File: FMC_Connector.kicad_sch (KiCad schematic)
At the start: 2 parts, among them J1 ASP-134488-01

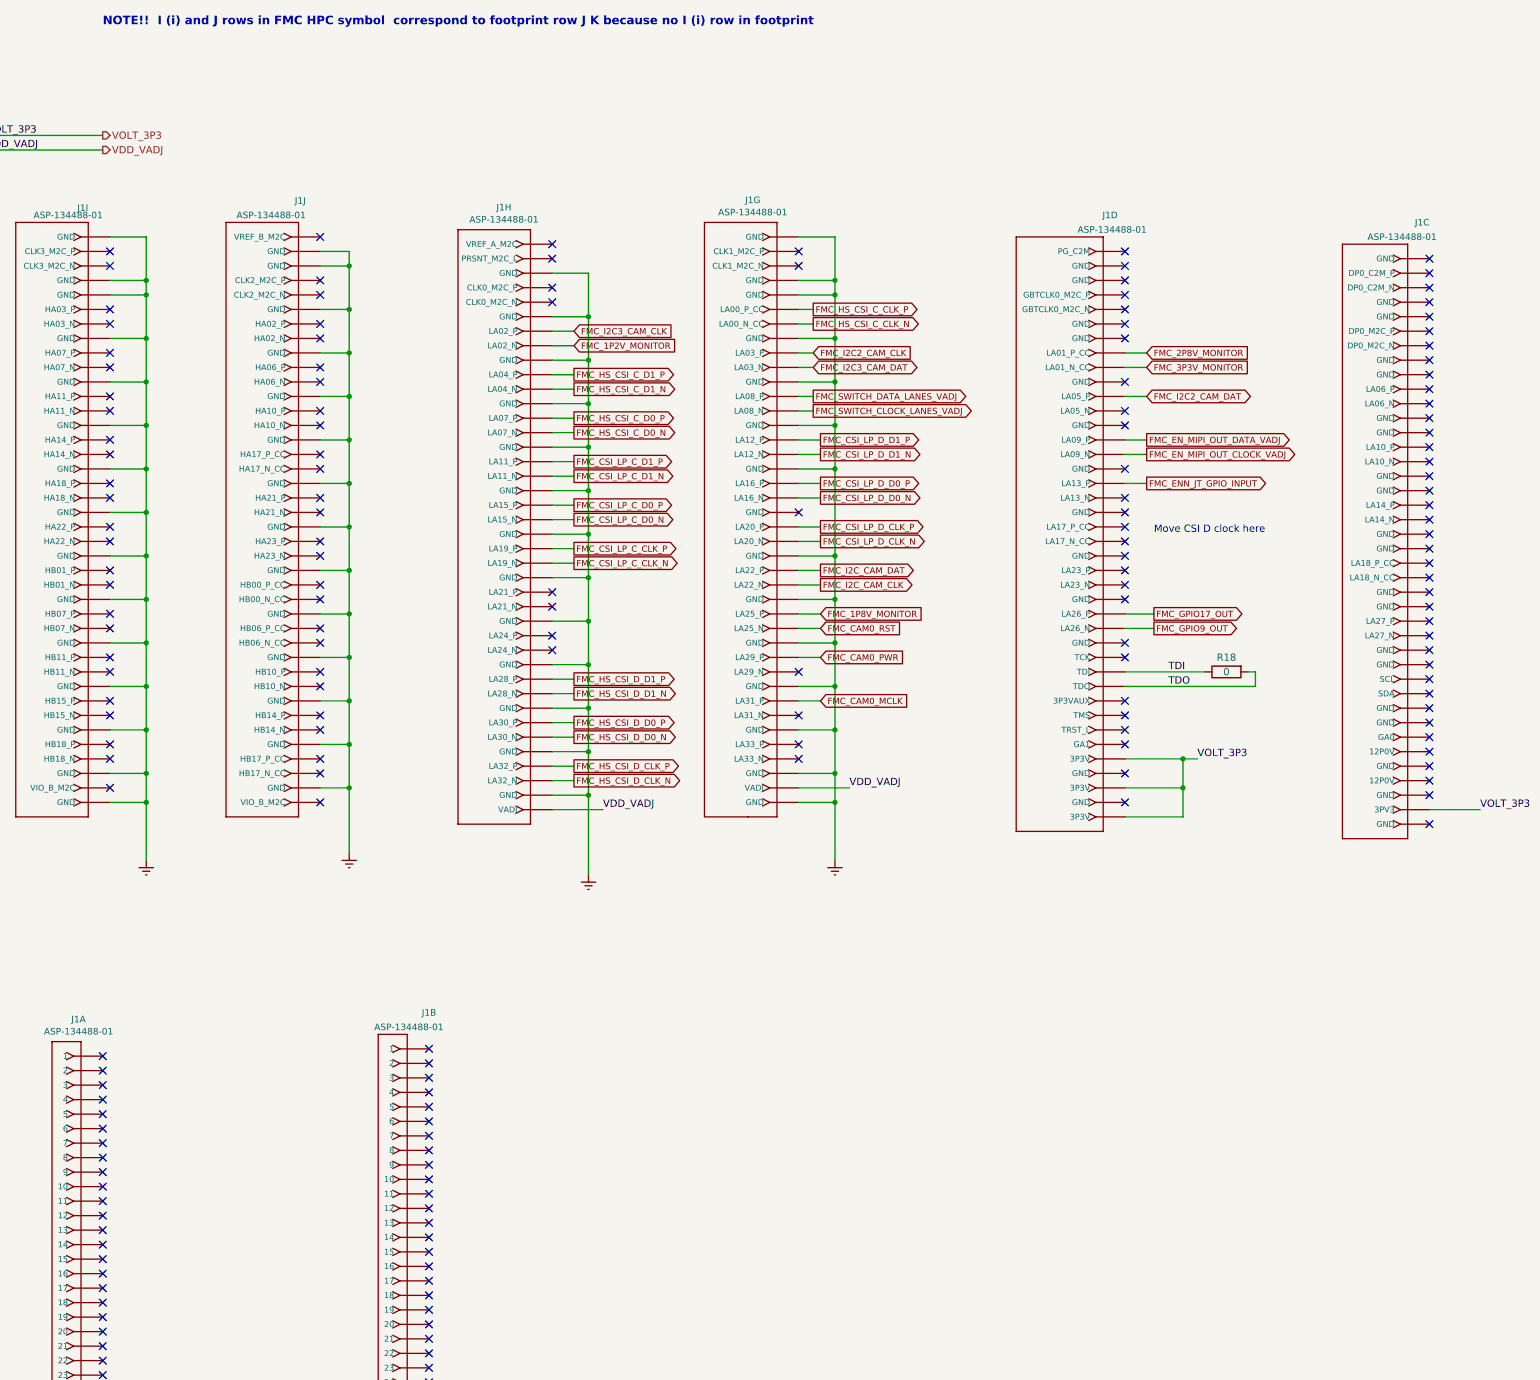
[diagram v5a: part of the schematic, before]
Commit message: Added debug points
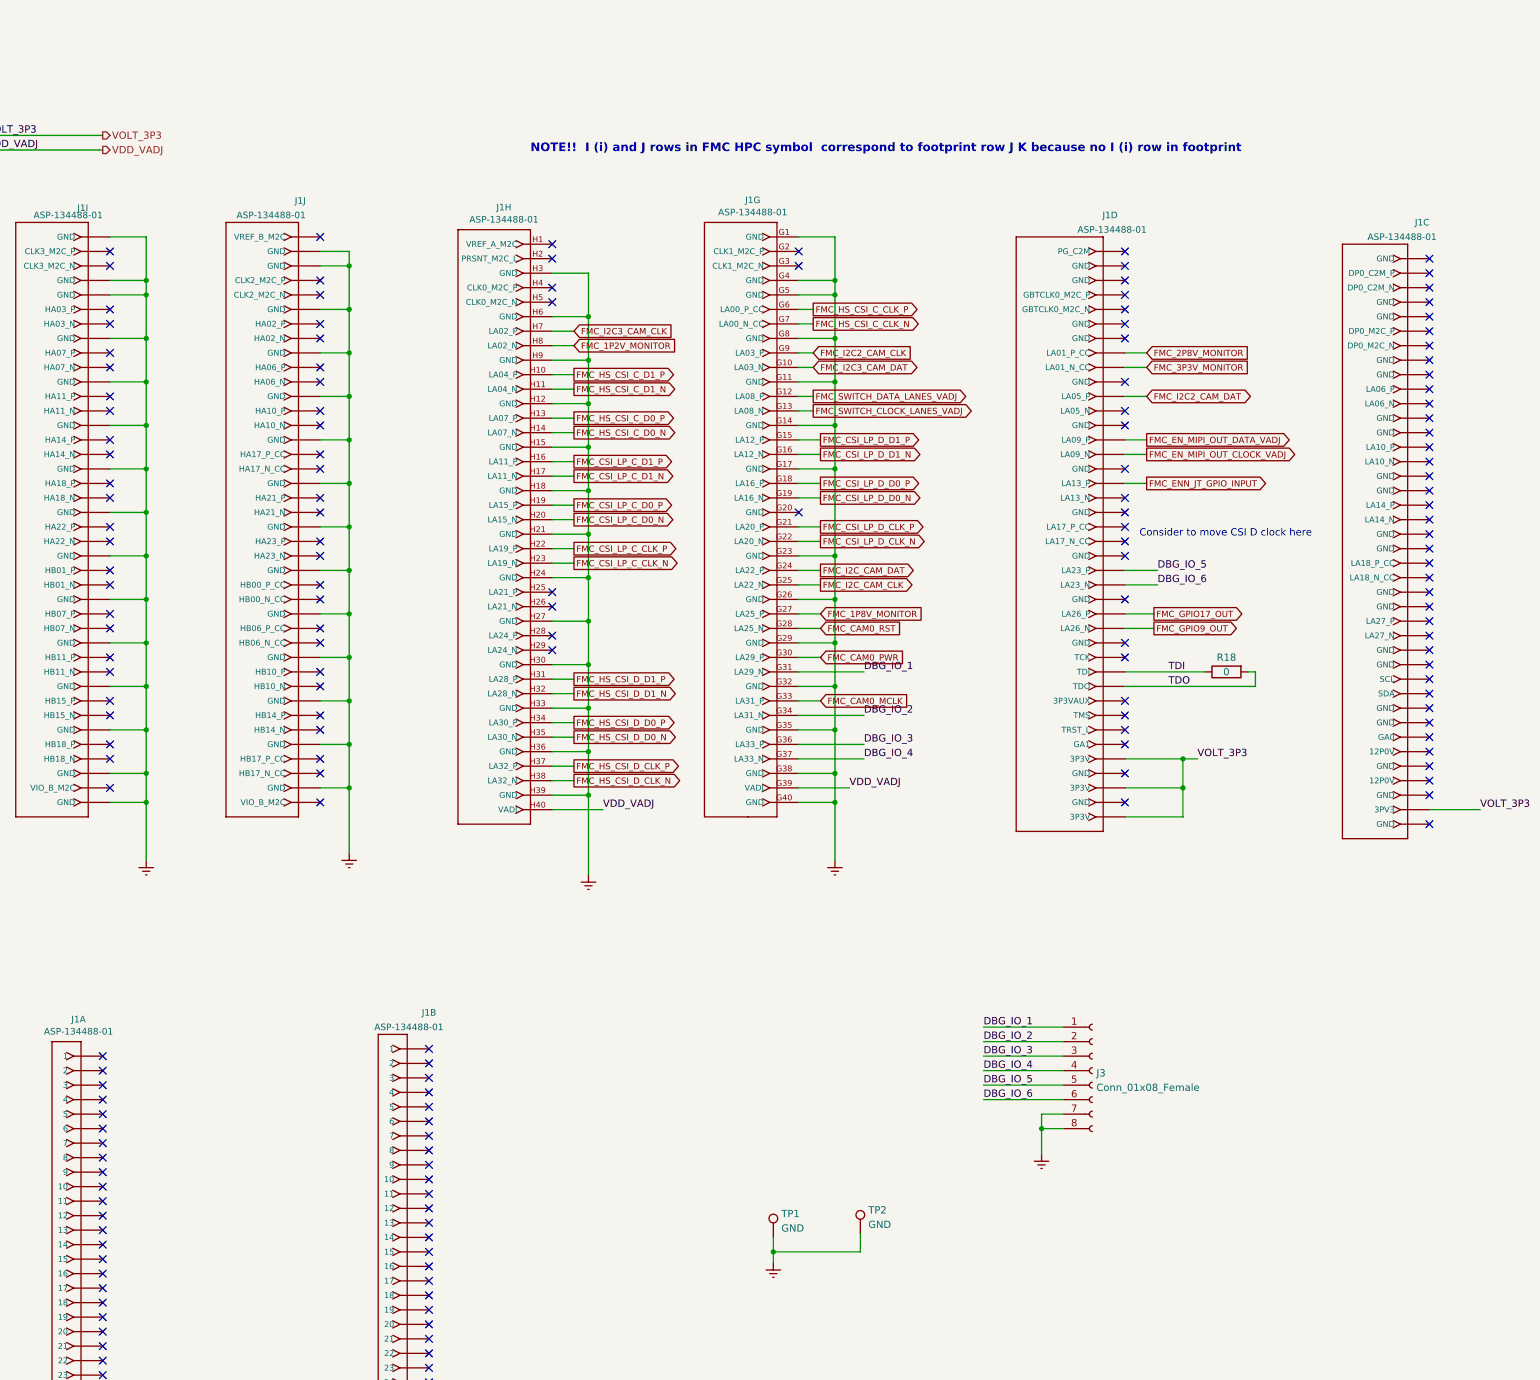
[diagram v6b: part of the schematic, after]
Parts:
- added J3: Conn_01x08_Female, Connector_PinHeader_2.54mm:PinHeader_2x04_P2.54mm_Vertical, symbol Connector:Conn_01x08_Female
- added TP1, TP2: GND, TestPoint:TestPoint_Keystone_5010-5014_Multipurpose, symbol Connector:TestPoint
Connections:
- net Earth: now also J3.7 (Pin_7), J3.8 (Pin_8), TP1.1, TP2.1
- net DBG_IO_5: now reaches J1.D23 (LA23_P)
- net DBG_IO_5: now also J3.5 (Pin_5)
- net DBG_IO_6: now reaches J1.D24 (LA23_N)
- net DBG_IO_6: now also J3.6 (Pin_6)
- net DBG_IO_1: now reaches J1.G31 (LA29_N)
- net DBG_IO_1: now also J3.1 (Pin_1)
- net DBG_IO_2: now reaches J1.G34 (LA31_N)
- net DBG_IO_2: now also J3.2 (Pin_2)
- net DBG_IO_3: now reaches J1.G36 (LA33_P)
- net DBG_IO_3: now also J3.3 (Pin_3)
- net DBG_IO_4: now reaches J1.G37 (LA33_N)
- net DBG_IO_4: now also J3.4 (Pin_4)
- no-connect marks 261 -> 255
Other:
- note added: "Consider to move CSI D clock here"
- note removed: "Move CSI D clock here"

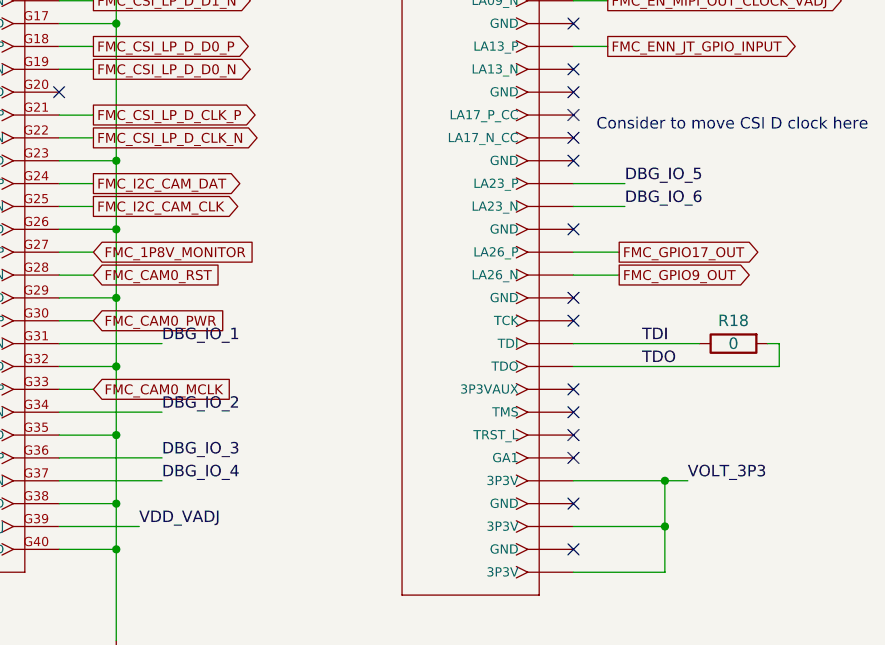
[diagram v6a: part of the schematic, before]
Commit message: Added debug connector
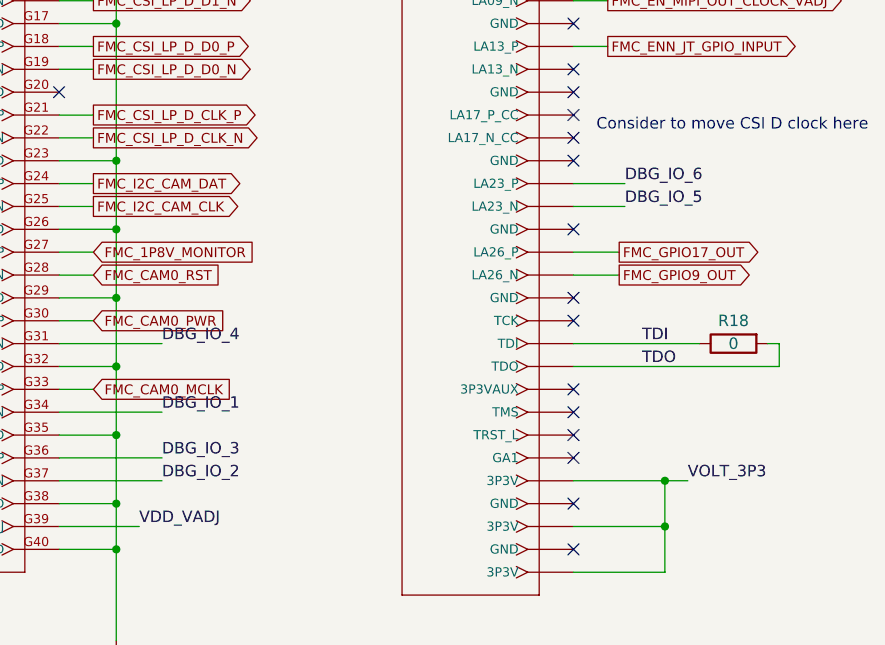
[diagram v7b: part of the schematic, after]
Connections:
- net DBG_IO_1: now also J1.G34 (LA31_N); no longer J1.G31 (LA29_N)
- net DBG_IO_2: now also J1.G37 (LA33_N); no longer J1.G34 (LA31_N)
- net DBG_IO_4: now also J1.G31 (LA29_N); no longer J1.G37 (LA33_N)
- net DBG_IO_5: now also J1.D24 (LA23_N); no longer J1.D23 (LA23_P)
- net DBG_IO_6: now also J1.D23 (LA23_P); no longer J1.D24 (LA23_N)
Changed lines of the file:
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@@
+    (effects (font (size 1.27 1.27)) (justify left bottom))
+  )
+  (label "DBG_IO_1" (at 168.91 118.11 0)
+    (effects (font (size 1.27 1.27)) (justify left bottom))
+  )
+  (label "DBG_IO_5" (at 220.345 95.25 0)
     (effects (font (size 1.27 1.27)) (justify left bottom))
   )
@@
     (effects (font (size 1.27 1.27)) (justify left bottom))
   )
-  (label "DBG_IO_5" (at 220.345 92.71 0)
+  (label "DBG_IO_3" (at 168.91 123.19 0)
     (effects (font (size 1.27 1.27)) (justify left bottom))
   )
@@
     (effects (font (size 1.27 1.27)) (justify left bottom))
   )
-  (label "DBG_IO_3" (at 168.91 123.19 0)
-    (effects (font (size 1.27 1.27)) (justify left bottom))
-  )
   (label "VDD_VADJ" (at 166.37 130.81 0)
     (effects (font (size 1.27 1.27)) (justify left bottom))
   )
-  (label "DBG_IO_4" (at 168.91 125.73 0)
+  (label "DBG_IO_6" (at 220.345 92.71 0)
+    (effects (font (size 1.27 1.27)) (justify left bottom))
+  )
+  (label "DBG_IO_4" (at 168.91 110.49 0)
     (effects (font (size 1.27 1.27)) (justify left bottom))
   )
@@
     (effects (font (size 1.27 1.27)) (justify left bottom))
   )
-  (label "DBG_IO_2" (at 189.865 175.26 0)
+  (label "DBG_IO_1" (at 189.865 172.72 0)
     (effects (font (size 1.27 1.27)) (justify left bottom))
   )
-  (label "DBG_IO_4" (at 189.865 180.34 0)
-    (effects (font (size 1.27 1.27)) (justify left bottom))
-  )
-  (label "DBG_IO_2" (at 168.91 118.11 0)
+  (label "DBG_IO_2" (at 189.865 175.26 0)
     (effects (font (size 1.27 1.27)) (justify left bottom))
   )
@@
     (effects (font (size 1.27 1.27)) (justify left bottom))
   )
-  (label "DBG_IO_5" (at 189.865 182.88 0)
+  (label "DBG_IO_6" (at 189.865 185.42 0)
     (effects (font (size 1.27 1.27)) (justify left bottom))
   )
-  (label "DBG_IO_6" (at 189.865 185.42 0)
+  (label "DBG_IO_5" (at 189.865 182.88 0)
     (effects (font (size 1.27 1.27)) (justify left bottom))
   )
@@
     (effects (font (size 1.27 1.27)) (justify left bottom))
   )
-  (label "VDD_VADJ" (at 123.19 134.62 0)
+  (label "DBG_IO_2" (at 168.91 125.73 0)
     (effects (font (size 1.27 1.27)) (justify left bottom))
   )
-  (label "DBG_IO_6" (at 220.345 95.25 0)
+  (label "VDD_VADJ" (at 123.19 134.62 0)
     (effects (font (size 1.27 1.27)) (justify left bottom))
   )
@@
     (effects (font (size 1.27 1.27)) (justify left bottom))
   )
-  (label "DBG_IO_1" (at 168.91 110.49 0)
-    (effects (font (size 1.27 1.27)) (justify left bottom))
-  )
   (label "VOLT_3P3" (at 15.24 16.51 0)
     (effects (font (size 1.27 1.27)) (justify left bottom))
   )
-  (label "DBG_IO_1" (at 189.865 172.72 0)
+  (label "DBG_IO_4" (at 189.865 180.34 0)
     (effects (font (size 1.27 1.27)) (justify left bottom))
   )

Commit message: Generated BOM, before Gerbers generation
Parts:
- J1: LCSC NeedToAsk -> C2762238
- J3: LCSC (none) -> DnP
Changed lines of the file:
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@@
       (effects (font (size 1.524 1.524)) hide)
     )
-    (property "LCSC" "NeedToAsk" (id 4) (at 25.4 234.95 0)
+    (property "LCSC" "C2762238" (id 4) (at 25.4 234.95 0)
       (effects (font (size 1.27 1.27)) hide)
     )
@@
       (effects (font (size 1.524 1.524)) hide)
     )
-    (property "LCSC" "NeedToAsk" (id 4) (at 87.63 227.33 0)
+    (property "LCSC" "C2762238" (id 4) (at 87.63 227.33 0)
       (effects (font (size 1.27 1.27)) hide)
     )
@@
       (effects (font (size 1.524 1.524)) hide)
     )
-    (property "LCSC" "NeedToAsk" (id 4) (at 262.89 88.9 0)
+    (property "LCSC" "C2762238" (id 4) (at 262.89 88.9 0)
       (effects (font (size 1.27 1.27)) hide)
     )
@@
       (effects (font (size 1.524 1.524)) hide)
     )
-    (property "LCSC" "NeedToAsk" (id 4) (at 209.55 87.63 0)
+    (property "LCSC" "C2762238" (id 4) (at 209.55 87.63 0)
       (effects (font (size 1.27 1.27)) hide)
     )
@@
       (effects (font (size 1.524 1.524)) hide)
     )
-    (property "LCSC" "NeedToAsk" (id 4) (at 377.19 87.63 0)
+    (property "LCSC" "C2762238" (id 4) (at 377.19 87.63 0)
       (effects (font (size 1.27 1.27)) hide)
     )
@@
       (effects (font (size 1.524 1.524)) hide)
     )
-    (property "LCSC" "NeedToAsk" (id 4) (at 322.58 87.63 0)
+    (property "LCSC" "C2762238" (id 4) (at 322.58 87.63 0)
       (effects (font (size 1.27 1.27)) hide)
     )
@@
       (effects (font (size 1.524 1.524)) hide)
     )
-    (property "LCSC" "NeedToAsk" (id 4) (at 142.24 85.09 0)
+    (property "LCSC" "C2762238" (id 4) (at 142.24 85.09 0)
       (effects (font (size 1.27 1.27)) hide)
     )
@@
       (effects (font (size 1.524 1.524)) hide)
     )
-    (property "LCSC" "NeedToAsk" (id 4) (at 96.52 87.63 0)
+    (property "LCSC" "C2762238" (id 4) (at 96.52 87.63 0)
       (effects (font (size 1.27 1.27)) hide)
     )
@@
       (effects (font (size 1.524 1.524)) hide)
     )
-    (property "LCSC" "NeedToAsk" (id 4) (at 31.75 85.09 0)
+    (property "LCSC" "C2762238" (id 4) (at 31.75 85.09 0)
       (effects (font (size 1.27 1.27)) hide)
     )
@@
       (effects (font (size 1.524 1.524)) hide)
     )
-    (property "LCSC" "NeedToAsk" (id 4) (at 68.58 85.09 0)
+    (property "LCSC" "C2762238" (id 4) (at 68.58 85.09 0)
       (effects (font (size 1.27 1.27)) hide)
     )
@@
       (effects (font (size 1.27 1.27)) hide)
     )
+    (property "LCSC" "DnP" (id 4) (at 208.915 180.34 0)
+      (effects (font (size 1.27 1.27)) hide)
+    )
